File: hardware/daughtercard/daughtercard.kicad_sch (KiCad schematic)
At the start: 48 parts, among them J1 Anzeige, J2 Bus in, J3 Bus out, J4 42V~ in, J5 42V~ out, J6 UPDI, Q1 BSS84, Q2 MMBT3904, Q3 MMBT3904, U1 ATtiny1616-SNR, U2 TP8485E-SR

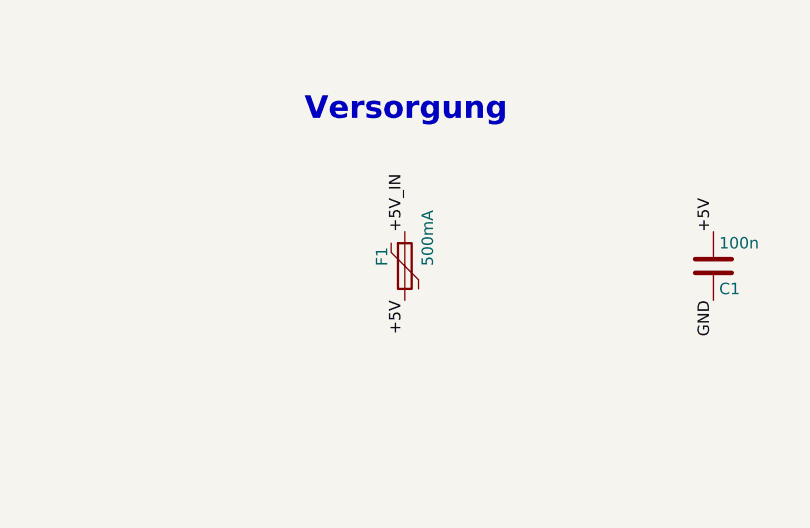
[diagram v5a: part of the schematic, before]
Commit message: PCB gerouted: alle Bahnen 0,5 mm ausser AC, schwarze Platine, Maker-Mark
Routing-Lauf auf der Betreiber-Platzierung (J1-J5 fix). FreeRouting 2.3.0
plus tools/finish_routes.py fuer die 1-2 Verbindungen, die FreeRouting
offen laesst (Rastersuch-Router). Masseflaeche F.Cu + B.Cu mit
Stitching-Raster und je einem Via an jedem GND-Pad.

Netzklassen (Betreiber-Vorgabe):
- alle Leiterbahnen 0,5 mm (an SOIC-Pins auf 0,375 mm verjuengt)
- nur AC1/AC2 1,5 mm
- GND ueber die Flaeche
Konsequenz +5V-Spannungsabfall bei 10 Modulen -> docs/jlc-bestueckung.md D-5.

Platzierung angepasst (ausserhalb J1-J5, vom Betreiber freigegeben):
- F1 von PTC 0,5 A auf 0-Ohm-Bruecke (R_1206 / 0R / C17888, D-3):
  F1 liegt im +5V-Durchgangspfad, ein PTC wuerde bei 10 Modulen ausloesen
- Q1-Q3, R7-R10, Status-LED aus dem AC-Korridor nach rechts gerueckt
  -> AC-Bahn haelt danach >= 0,55 mm Kupfer zu jeder Logikbahn
- J6 (UPDI) unter U1

Schaltplan: F1 -> krone:R "0R"; Footprint-Pfade der .kicad_pcb per
UUID-Remapping auf den neu erzeugten Schaltplan gezogen (Platzierung und
Routing bleiben erhalten). ERC 0/0, DRC 0/0.

Fertigung:
- Lagenaufbau schwarze Loetstoppmaske / weisser Bestueckungsdruck
- Maker-Kennzeichnung auf B.SilkS: GitHub-Marke (octicon mark-github, aus
  SVG getraced, footprints/logos.pretty/Logo_GitHub) + Text "TenOfNine"
- tools/add_silk_marks.py setzt beides idempotent

Neu: tools/finish_routes.py, tools/add_silk_marks.py, fp-lib-table,
footprints/logos.pretty/. setup.sh: python3-numpy fuer finish_routes.
Schaltplan v0.7, Doku (Layout, JLC, Toolchain, Projektstand) fortgeschrieben.

Co-Authored-By: Claude Sonnet 5 <noreply@anthropic.com>
Claude-Session: https://claude.ai/code/session_01UsXTvE3jGgoK5Hec7hVbyD
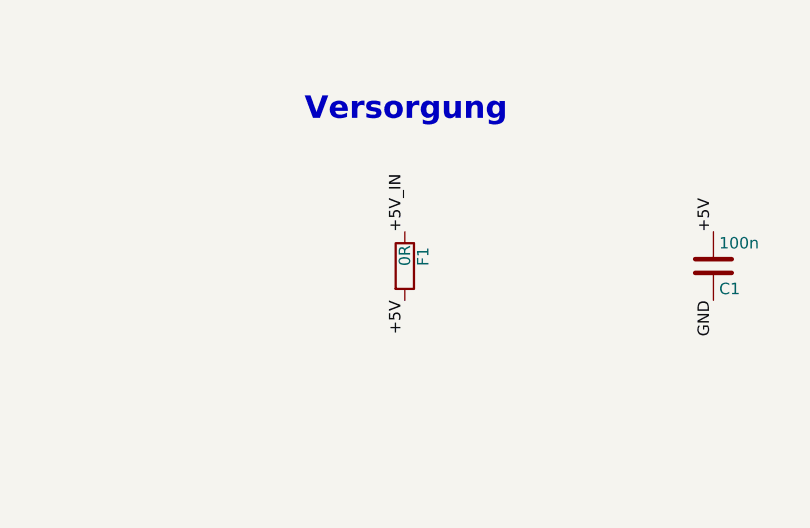
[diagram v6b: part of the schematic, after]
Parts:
- removed F1: 500mA, Fuse:Fuse_1206_3216Metric, symbol krone:Polyfuse
- added F1: 0R, Resistor_SMD:R_1206_3216Metric, symbol krone:R
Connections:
- net +5V: now also F1.2
- net +5V_IN: now also F1.1
